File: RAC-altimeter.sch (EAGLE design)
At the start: 3 parts, among them IC1 MAX32660GWE+, IC2 BMP388, Y1 32.768kHz

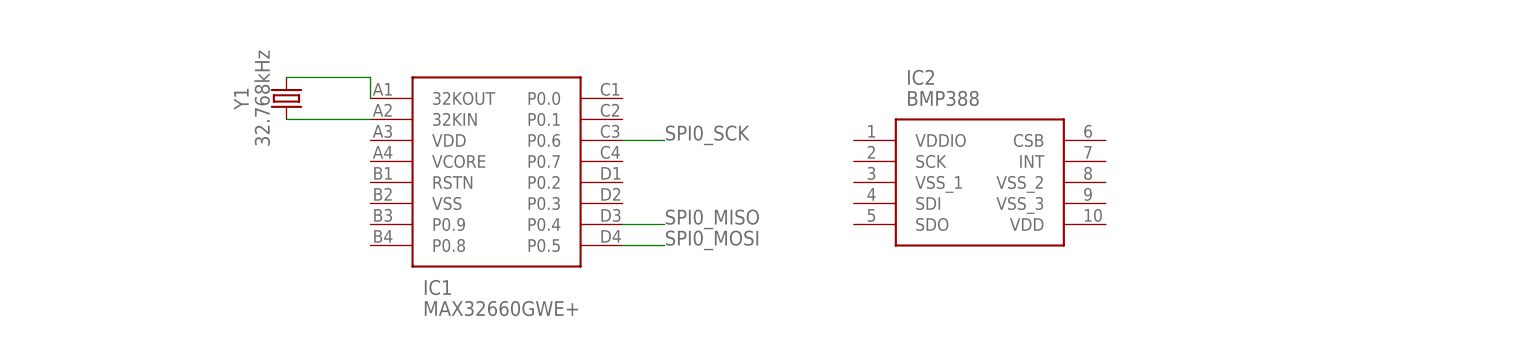
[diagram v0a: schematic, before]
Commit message: Added decoupling capacitors to BMP388
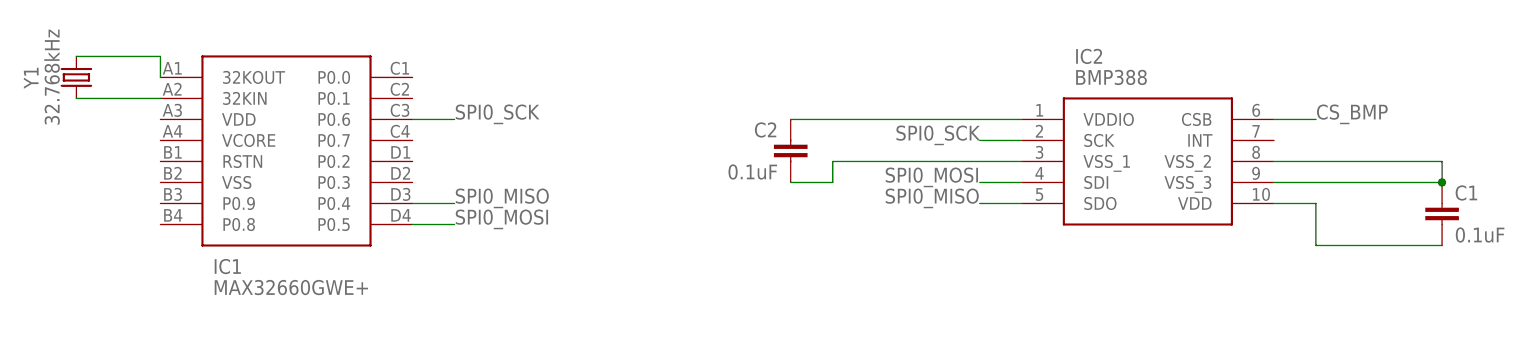
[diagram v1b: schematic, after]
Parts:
- added C1, C2: 0.1uF, SparkFun-Capacitors:0.1UF-0603-25V-(+80/-20%)
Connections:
- new net CS_BMP: IC2.CSB
- new net N$3: C1.1, IC2.VSS_2, IC2.VSS_3
- new net N$4: C1.2, IC2.VDD
- new net N$5: C2.1, IC2.VDDIO
- new net N$6: C2.2, IC2.VSS_1
- net SPI0_MISO: now also IC2.SDO
- net SPI0_MOSI: now also IC2.SDI
- net SPI0_SCK: now also IC2.SCK
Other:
- moved on the sheet: IC1, IC2, Y1
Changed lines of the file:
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@@
 <layer number="230" name="230bmp" color="7" fill="1" visible="yes" active="yes"/>
 <layer number="231" name="231bmp" color="7" fill="1" visible="yes" active="yes"/>
+<layer number="232" name="Eagle3D_PG2" color="7" fill="1" visible="no" active="no"/>
+<layer number="233" name="Eagle3D_PG3" color="7" fill="1" visible="no" active="no"/>
 <layer number="248" name="Housing" color="7" fill="1" visible="yes" active="yes"/>
 <layer number="249" name="Edge" color="7" fill="1" visible="yes" active="yes"/>
@@
 <part name="IC2" library="BMP388" deviceset="BMP388" device=""/>
 <part name="Y1" library="ST2012SB32768B0HPWB4" deviceset="ST2012SB32768B0HPWB4" device="" value="32.768kHz"/>
+<part name="C1" library="SparkFun-Capacitors" deviceset="0.1UF" device="-0603-25V-(+80/-20%)" value="0.1uF"/>
+<part name="C2" library="SparkFun-Capacitors" deviceset="0.1UF" device="-0603-25V-(+80/-20%)" value="0.1uF"/>
 </parts>
 <sheets>
@@
 </plain>
 <instances>
-<instance part="IC1" gate="G$1" x="53.34" y="68.58" smashed="yes">
-<attribute name="NAME" x="59.69" y="45.72" size="1.778" layer="95" align="center-left"/>
-<attribute name="VALUE" x="59.69" y="43.18" size="1.778" layer="96" align="center-left"/>
+<instance part="IC1" gate="G$1" x="27.94" y="71.12" smashed="yes">
+<attribute name="NAME" x="34.29" y="48.26" size="1.778" layer="95" align="center-left"/>
+<attribute name="VALUE" x="34.29" y="45.72" size="1.778" layer="96" align="center-left"/>
 </instance>
-<instance part="IC2" gate="G$1" x="111.76" y="63.5" smashed="yes">
-<attribute name="NAME" x="118.11" y="71.12" size="1.778" layer="95" align="center-left"/>
-<attribute name="VALUE" x="118.11" y="68.58" size="1.778" layer="96" align="center-left"/>
+<instance part="IC2" gate="G$1" x="132.08" y="66.04" smashed="yes">
+<attribute name="NAME" x="138.43" y="73.66" size="1.778" layer="95" align="center-left"/>
+<attribute name="VALUE" x="138.43" y="71.12" size="1.778" layer="96" align="center-left"/>
 </instance>
-<instance part="Y1" gate="G$1" x="43.18" y="68.58" smashed="yes" rot="R90">
-<attribute name="NAME" x="38.608" y="68.58" size="1.778" layer="95" font="vector" rot="R90" align="bottom-center"/>
-<attribute name="VALUE" x="41.148" y="68.58" size="1.778" layer="96" font="vector" rot="R270" align="top-center"/>
+<instance part="Y1" gate="G$1" x="17.78" y="71.12" smashed="yes" rot="R90">
+<attribute name="NAME" x="13.208" y="71.12" size="1.778" layer="95" font="vector" rot="R90" align="bottom-center"/>
+<attribute name="VALUE" x="15.748" y="71.12" size="1.778" layer="96" font="vector" rot="R270" align="top-center"/>
+</instance>
+<instance part="C1" gate="G$1" x="182.88" y="53.34" smashed="yes">
+<attribute name="NAME" x="184.404" y="56.261" size="1.778" layer="95" font="vector"/>
+<attribute name="VALUE" x="184.404" y="51.181" size="1.778" layer="96" font="vector"/>
+</instance>
+<instance part="C2" gate="G$1" x="104.14" y="60.96" smashed="yes" rot="MR0">
+<attribute name="NAME" x="102.616" y="63.881" size="1.778" layer="95" font="vector" rot="MR0"/>
+<attribute name="VALUE" x="102.616" y="58.801" size="1.778" layer="96" font="vector" rot="MR0"/>
 </instance>
 </instances>
@@
 <segment>
 <pinref part="Y1" gate="G$1" pin="2"/>
-<wire x1="43.18" y1="71.12" x2="53.34" y2="71.12" width="0.1524" layer="91"/>
+<wire x1="17.78" y1="73.66" x2="27.94" y2="73.66" width="0.1524" layer="91"/>
 <pinref part="IC1" gate="G$1" pin="32KOUT"/>
-<wire x1="53.34" y1="71.12" x2="53.34" y2="68.58" width="0.1524" layer="91"/>
+<wire x1="27.94" y1="73.66" x2="27.94" y2="71.12" width="0.1524" layer="91"/>
 </segment>
 </net>
@@
 <pinref part="Y1" gate="G$1" pin="1"/>
 <pinref part="IC1" gate="G$1" pin="32KIN"/>
-<wire x1="43.18" y1="66.04" x2="53.34" y2="66.04" width="0.1524" layer="91"/>
+<wire x1="17.78" y1="68.58" x2="27.94" y2="68.58" width="0.1524" layer="91"/>
 </segment>
 </net>
@@
 <segment>
 <pinref part="IC1" gate="G$1" pin="P0.6"/>
-<wire x1="83.82" y1="63.5" x2="88.9" y2="63.5" width="0.1524" layer="91"/>
-<label x="88.9" y="63.5" size="1.778" layer="95"/>
+<wire x1="58.42" y1="66.04" x2="63.5" y2="66.04" width="0.1524" layer="91"/>
+<label x="63.5" y="66.04" size="1.778" layer="95"/>
+</segment>
+<segment>
+<pinref part="IC2" gate="G$1" pin="SCK"/>
+<wire x1="132.08" y1="63.5" x2="127" y2="63.5" width="0.1524" layer="91"/>
+<label x="127" y="63.5" size="1.778" layer="95" rot="MR0"/>
 </segment>
 </net>
@@
 <segment>
 <pinref part="IC1" gate="G$1" pin="P0.4"/>
-<wire x1="83.82" y1="53.34" x2="88.9" y2="53.34" width="0.1524" layer="91"/>
-<label x="88.9" y="53.34" size="1.778" layer="95"/>
+<wire x1="58.42" y1="55.88" x2="63.5" y2="55.88" width="0.1524" layer="91"/>
+<label x="63.5" y="55.88" size="1.778" layer="95"/>
+</segment>
+<segment>
+<pinref part="IC2" gate="G$1" pin="SDO"/>
+<wire x1="132.08" y1="55.88" x2="127" y2="55.88" width="0.1524" layer="91"/>
+<label x="127" y="55.88" size="1.778" layer="95" rot="MR0"/>
 </segment>
 </net>
@@
 <segment>
 <pinref part="IC1" gate="G$1" pin="P0.5"/>
-<wire x1="83.82" y1="50.8" x2="88.9" y2="50.8" width="0.1524" layer="91"/>
-<label x="88.9" y="50.8" size="1.778" layer="95"/>
+<wire x1="58.42" y1="53.34" x2="63.5" y2="53.34" width="0.1524" layer="91"/>
+<label x="63.5" y="53.34" size="1.778" layer="95"/>
+</segment>
+<segment>
+<pinref part="IC2" gate="G$1" pin="SDI"/>
+<wire x1="132.08" y1="58.42" x2="127" y2="58.42" width="0.1524" layer="91"/>
+<label x="127" y="58.42" size="1.778" layer="95" rot="MR0"/>
 </segment>
 </net>
+<net name="N$3" class="0">
+<segment>
+<pinref part="IC2" gate="G$1" pin="VSS_3"/>
+<pinref part="C1" gate="G$1" pin="1"/>
+<wire x1="162.56" y1="58.42" x2="182.88" y2="58.42" width="0.1524" layer="91"/>
+<pinref part="IC2" gate="G$1" pin="VSS_2"/>
+<wire x1="162.56" y1="60.96" x2="182.88" y2="60.96" width="0.1524" layer="91"/>
+<wire x1="182.88" y1="60.96" x2="182.88" y2="58.42" width="0.1524" layer="91"/>
+<junction x="182.88" y="58.42"/>
+</segment>
+</net>
+<net name="N$5" class="0">
+<segment>
+<pinref part="C2" gate="G$1" pin="1"/>
+<pinref part="IC2" gate="G$1" pin="VDDIO"/>
+<wire x1="104.14" y1="66.04" x2="132.08" y2="66.04" width="0.1524" layer="91"/>
+</segment>
+</net>
+<net name="N$4" class="0">
+<segment>
+<pinref part="IC2" gate="G$1" pin="VDD"/>
+<wire x1="162.56" y1="55.88" x2="167.64" y2="55.88" width="0.1524" layer="91"/>
+<wire x1="167.64" y1="55.88" x2="167.64" y2="50.8" width="0.1524" layer="91"/>
+<pinref part="C1" gate="G$1" pin="2"/>
+<wire x1="167.64" y1="50.8" x2="182.88" y2="50.8" width="0.1524" layer="91"/>
+</segment>
+</net>
+<net name="N$6" class="0">
+<segment>
+<pinref part="IC2" gate="G$1" pin="VSS_1"/>
+<wire x1="132.08" y1="60.96" x2="109.22" y2="60.96" width="0.1524" layer="91"/>
+<wire x1="109.22" y1="60.96" x2="109.22" y2="58.42" width="0.1524" layer="91"/>
+<pinref part="C2" gate="G$1" pin="2"/>
+<wire x1="109.22" y1="58.42" x2="104.14" y2="58.42" width="0.1524" layer="91"/>
+</segment>
+</net>
+<net name="CS_BMP" class="0">
+<segment>
+<pinref part="IC2" gate="G$1" pin="CSB"/>
+<wire x1="162.56" y1="66.04" x2="167.64" y2="66.04" width="0.1524" layer="91"/>
+<label x="167.64" y="66.04" size="1.778" layer="95"/>
+</segment>
+</net>

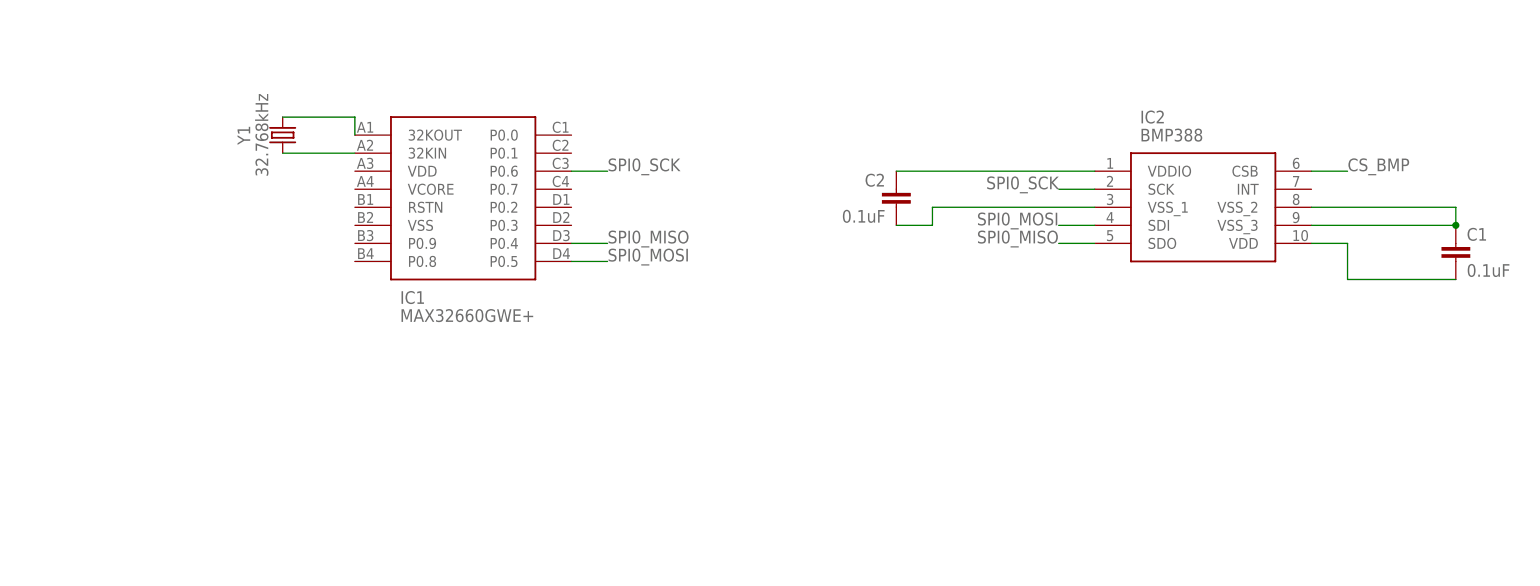
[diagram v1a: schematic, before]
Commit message: Added SD Card, rewired BMP388 for I2C
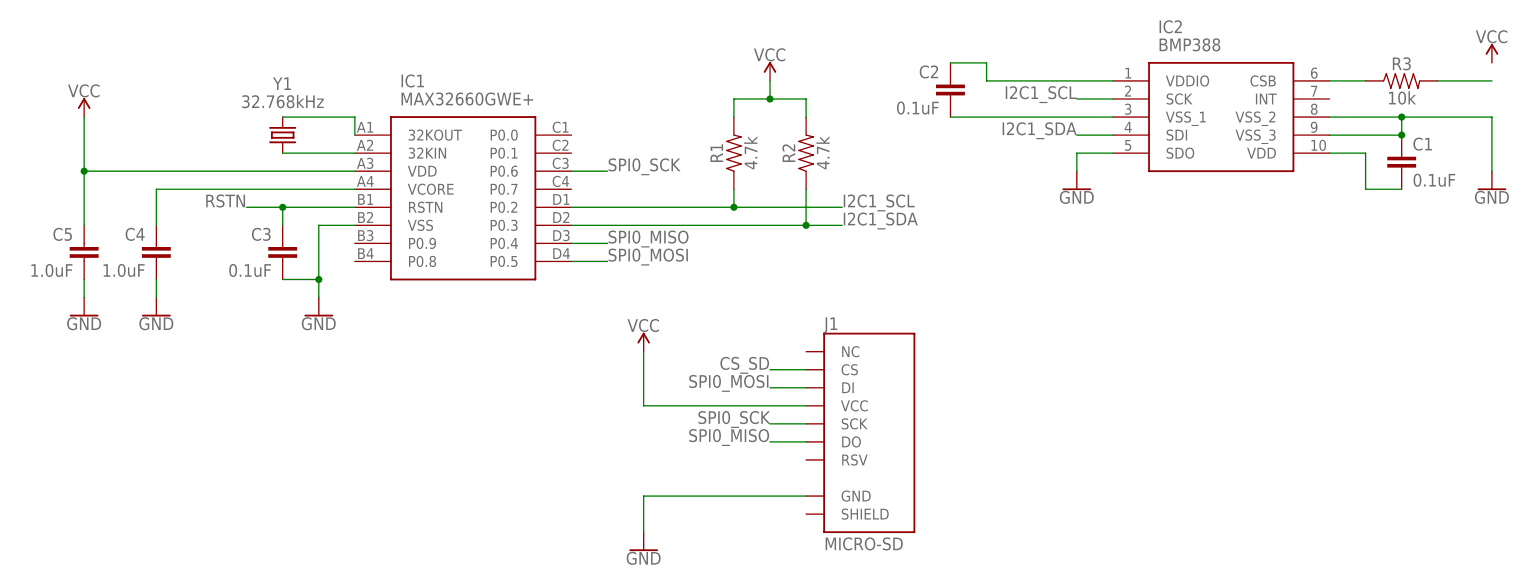
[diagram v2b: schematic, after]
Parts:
- added C3: 0.1uF, SparkFun-Capacitors:0.1UF-0603-25V-(+80/-20%)
- added C4, C5: 1.0uF, SparkFun-Capacitors:1.0UF-0603-16V-10%
- added J1: MICRO-SD, SparkFun-Connectors:MICRO-SD_CARD_SOCKETTINY
- added R1, R2: 4.7k, SparkFun-Resistors:4.7KOHM-0603-1/10W-1%
- added R3: 10k, SparkFun-Resistors:10KOHM-0603-1/10W-1%
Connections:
- removed net CS_BMP: IC2.CSB
- new net BMP_CS: IC2.CSB, R3.1
- new net CS_SD: J1.CS
- new net GND: C1.1, C3.2, C4.2, C5.2, IC1.VSS, IC2.SDO, IC2.VSS_2, IC2.VSS_3, J1.GND
- new net I2C1_SCL: IC1.P0.2, IC2.SCK, R1.1
- new net I2C1_SDA: IC1.P0.3, IC2.SDI, R2.1
- new net RSTN: C3.1, IC1.RSTN
- new net VCC: C5.1, IC1.VDD, J1.VCC, R1.2, R2.2
- new net VCORE: C4.1, IC1.VCORE
- net N$3: now also R3.2; no longer C1.1, IC2.VSS_2, IC2.VSS_3
- net SPI0_MISO: now also J1.DO; no longer IC2.SDO
- net SPI0_MOSI: now also J1.DI; no longer IC2.SDI
- net SPI0_SCK: now also J1.SCK; no longer IC2.SCK
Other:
- moved on the sheet: C1, C2, IC2

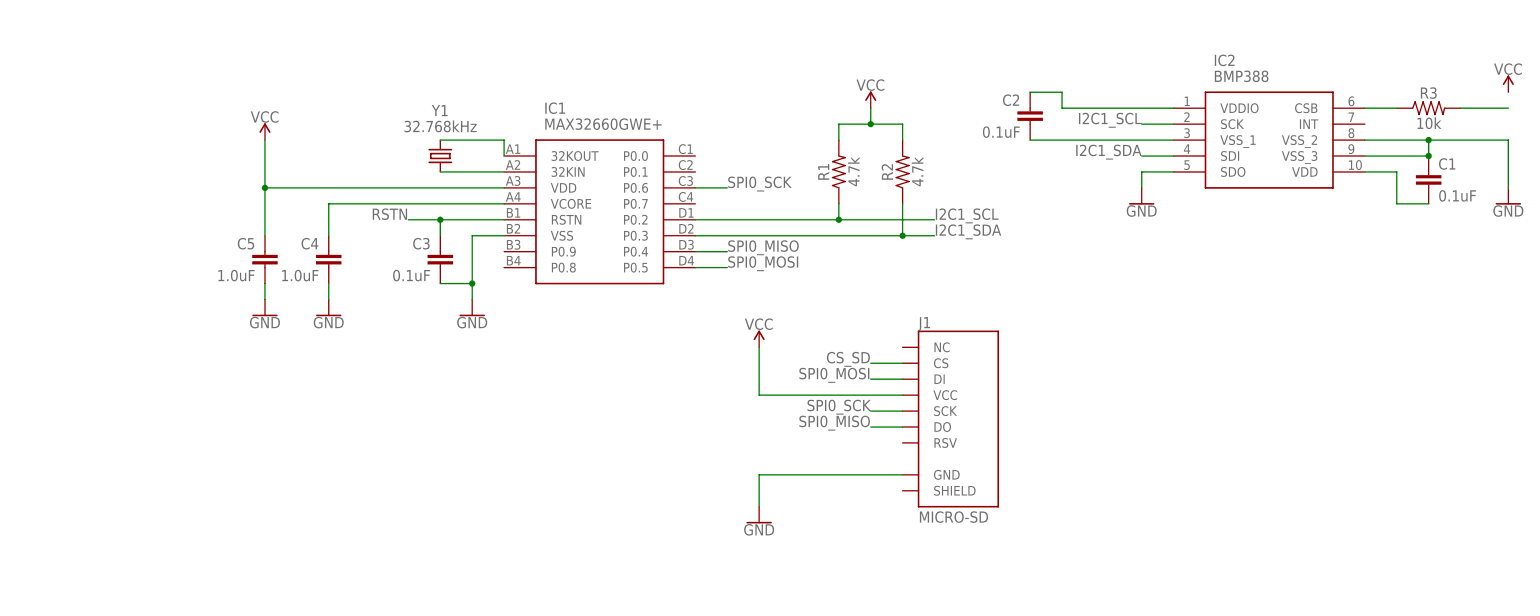
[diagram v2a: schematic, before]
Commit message: Replaced MAX32660 with STM32L412 MCU
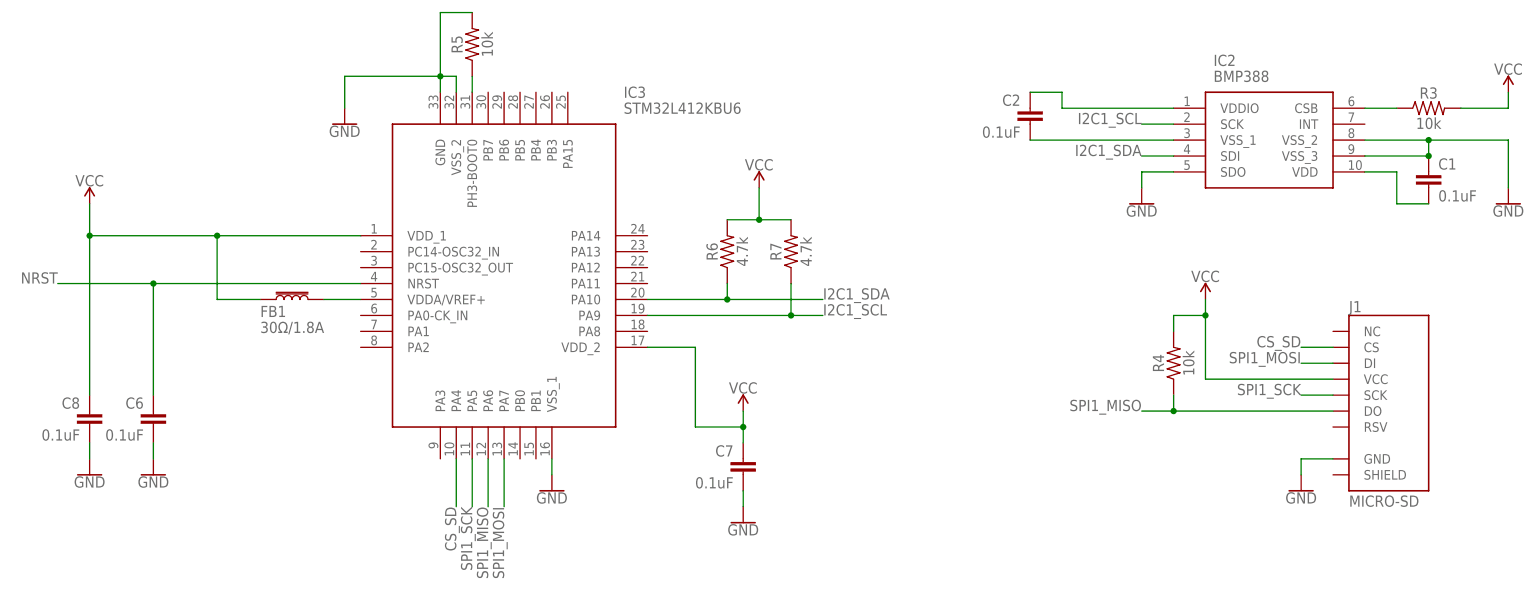
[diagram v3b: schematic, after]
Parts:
- removed C3: 0.1uF, SparkFun-Capacitors:0.1UF-0603-25V-(+80/-20%)
- removed C4, C5: 1.0uF, SparkFun-Capacitors:1.0UF-0603-16V-10%
- removed IC1: MAX32660GWE+, MAX32660GWE+:MAX32660GWE+
- removed R1, R2: 4.7k, SparkFun-Resistors:4.7KOHM-0603-1/10W-1%
- removed Y1: 32.768kHz, ST2012SB32768B0HPWB4:ST2012SB32768B0HPWB4
- added C6, C7, C8: 0.1uF, SparkFun-Capacitors:0.1UF-0603-25V-(+80/-20%)
- added FB1: 30Ω/1.8A, SparkFun-Coils:FERRITE_BEAD-0603
- added IC3: STM32L412KBU6, STM32L412KBU6:STM32L412KBU6
- added R4, R5: 10k, SparkFun-Resistors:10KOHM-0603-1/10W-1%
- added R6, R7: 4.7k, SparkFun-Resistors:4.7KOHM-0603-1/10W-1%
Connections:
- removed net N$1: IC1.32KOUT, Y1.2
- removed net N$2: IC1.32KIN, Y1.1
- removed net RSTN: C3.1, IC1.RSTN
- removed net SPI0_MISO: IC1.P0.4, J1.DO
- removed net SPI0_MOSI: IC1.P0.5, J1.DI
- removed net SPI0_SCK: IC1.P0.6, J1.SCK
- removed net VCORE: C4.1, IC1.VCORE
- new net N$7: FB1.2, IC3.VDDA/VREF+
- new net NRST: C6.1, IC3.NRST
- new net SPI1_MISO: IC3.PA6, J1.DO, R4.1
- new net SPI1_MOSI: IC3.PA7, J1.DI
- new net SPI1_SCK: IC3.PA5, J1.SCK
- net CS_SD: now also IC3.PA4
- net GND: now also C6.2, C7.2, C8.2, IC3.GND, IC3.VSS_1, IC3.VSS_2, R5.2; no longer C3.2, C4.2, C5.2, IC1.VSS
- net I2C1_SCL: now also IC3.PA9, R7.1; no longer IC1.P0.2, R1.1
- net I2C1_SDA: now also IC3.PA10, R6.1; no longer IC1.P0.3, R2.1
- net N$3: now also IC3.PH3-BOOT0, R5.1; no longer R3.2
- net VCC: now also C7.1, C8.1, FB1.1, IC3.VDD_1, IC3.VDD_2, R3.2, R4.2, R6.2, R7.2; no longer C5.1, IC1.VDD, R1.2, R2.2
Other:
- moved on the sheet: J1
